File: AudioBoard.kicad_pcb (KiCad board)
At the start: 2 copper layers, 100 x 100 mm, 77 parts, among them IC1 AMS1117-5.0, IC2 PCM5102APWR, IC3 PCM1803ADBR, J1 I2S2_OPT, J10 POT, J11 POT, J12 Raspberry_Pi_2_3, J13 57PC5F, J14 57PC5F, J15 RCA_2x2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

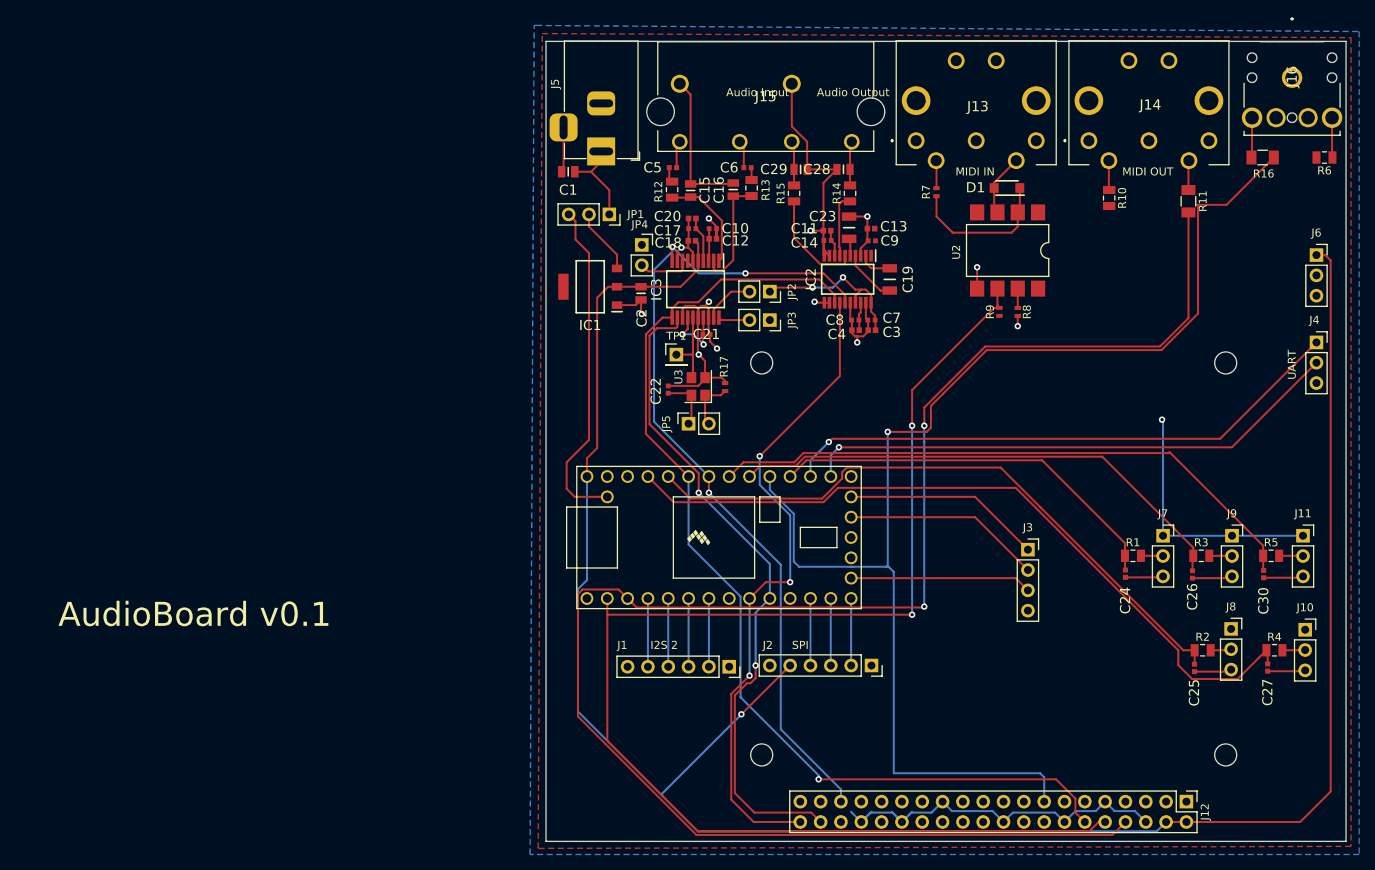
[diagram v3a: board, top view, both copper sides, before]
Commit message: Added mounting holes and wrapped up PCB design.
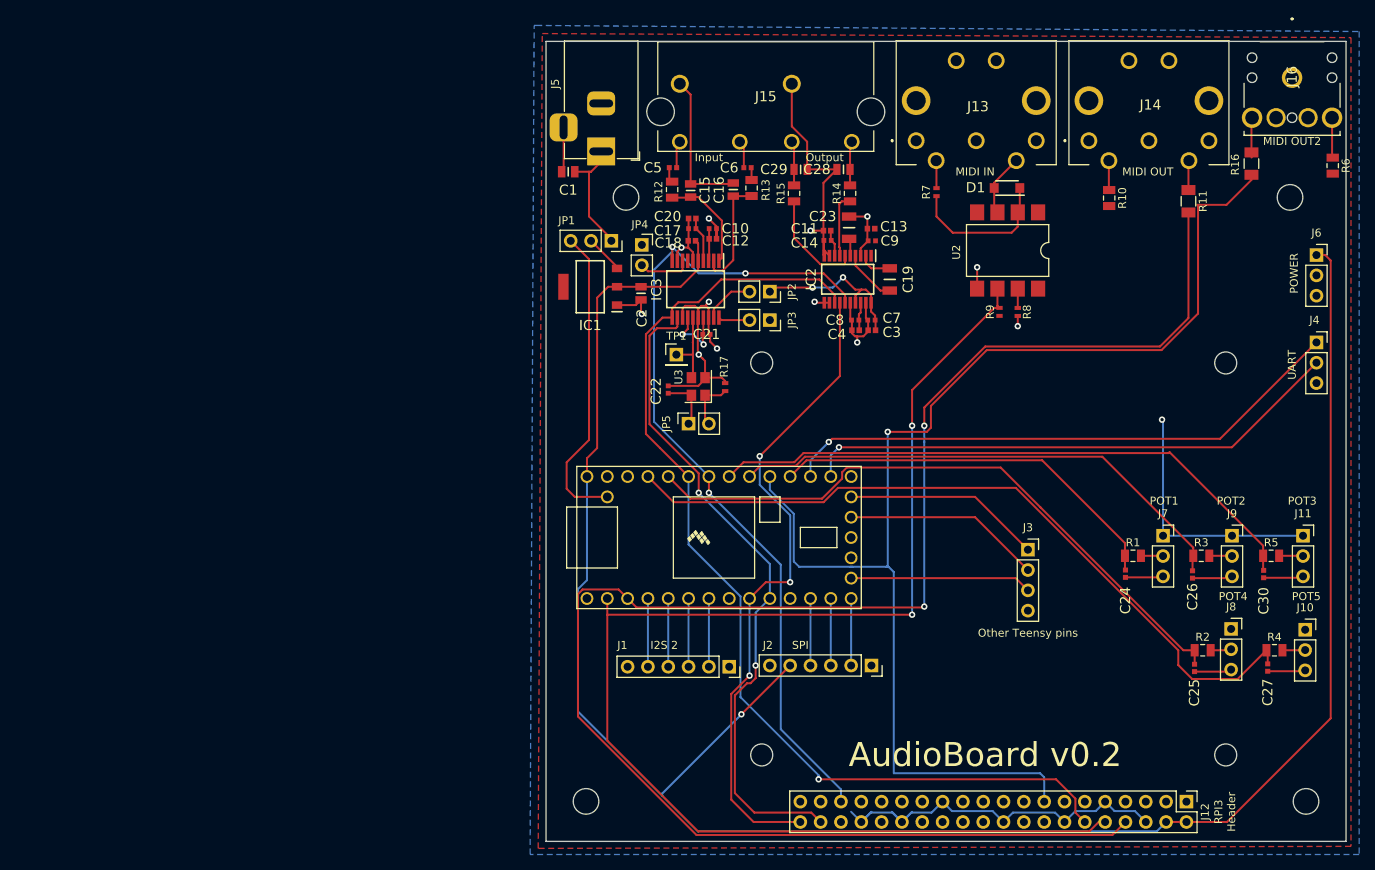
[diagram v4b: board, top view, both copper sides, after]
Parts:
- added REF**: MountingHole_3.2mm_M3, MountingHole:MountingHole_3.2mm_M3, F.Cu at (143.0, 69.5)
- added REF**: MountingHole_3.2mm_M3, MountingHole:MountingHole_3.2mm_M3, F.Cu at (60.0, 69.5)
- added REF**: MountingHole_3.2mm_M3, MountingHole:MountingHole_3.2mm_M3, F.Cu at (145.0, 145.0)
- added REF**: MountingHole_3.2mm_M3, MountingHole:MountingHole_3.2mm_M3, F.Cu at (55.0, 145.0)
- moved JP1 3.31 mm to (58.2, 74.9)
- moved R16 1.59 mm to (138.2, 65.3), turned to 270 degrees
- moved R6 1.45 mm to (148.3, 65.5), turned to 270 degrees
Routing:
- net +5V: track 264.2 -> 258.8 mm
- net /DC_IN: track 11.4 -> 14.9 mm
- net Net-(IC1-Pad3): track 8.20 -> 4.80 mm
- net /V_USB: track 42.0 -> 38.6 mm
- net /MIDI_OUT2: track 161.5 -> 158.2 mm
- net Net-(J16-Pad2): track 5.01 -> 4.49 mm
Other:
- board text added: "AudioBoard v0.2"
- board text added: "Input"
- board text added: "MIDI OUT2"
- board text added: "Other Teensy pins"
- board text added: "Output"
- board text added: "POT1"
- board text added: "POT2"
- board text added: "POT3"
- board text added: "POT4"
- board text added: "POT5"
- board text added: "POWER"
- board text added: "RPI3 Header"
- board text removed: "Audio Input"
- board text removed: "Audio Output"
- board text removed: "AudioBoard v0.1"

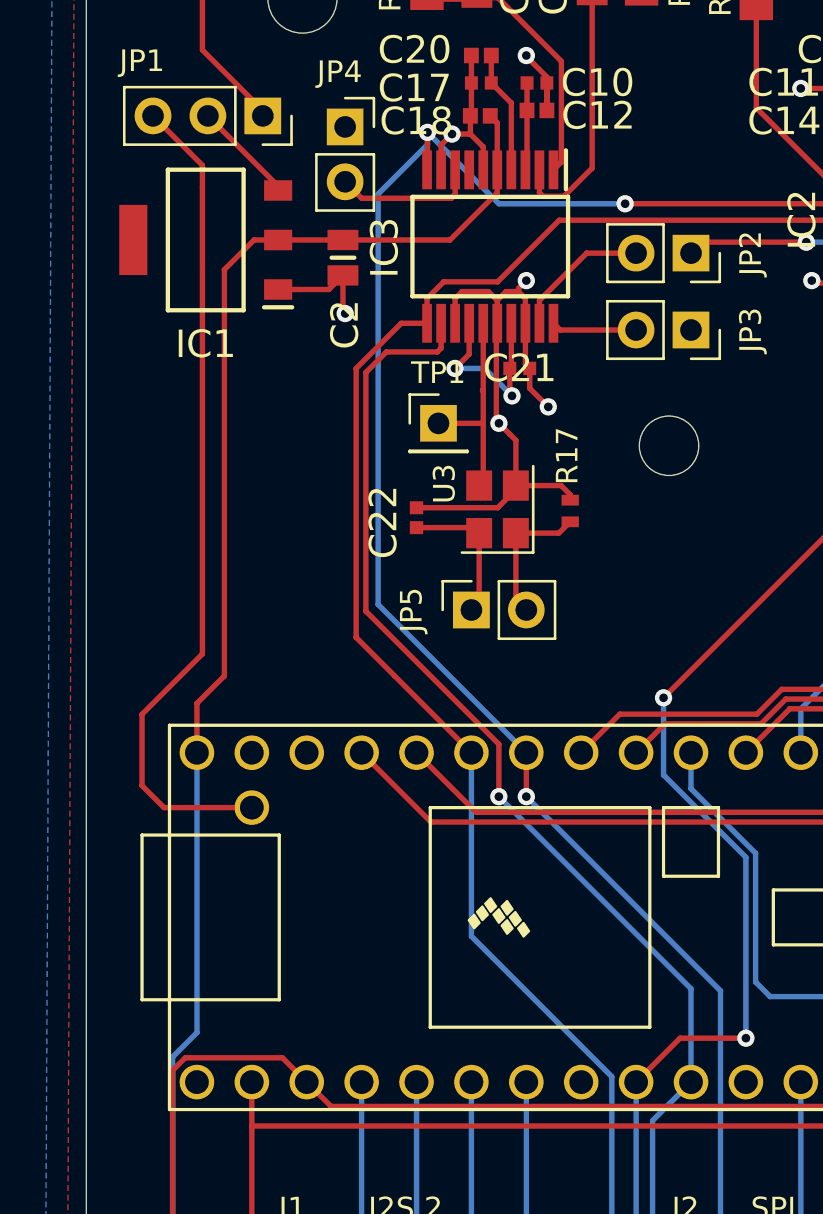
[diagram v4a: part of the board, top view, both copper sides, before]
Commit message: Added pin header for I2S input, to connect an external ADC (the PCM1803ADBR was unavailable at the time of ordering).
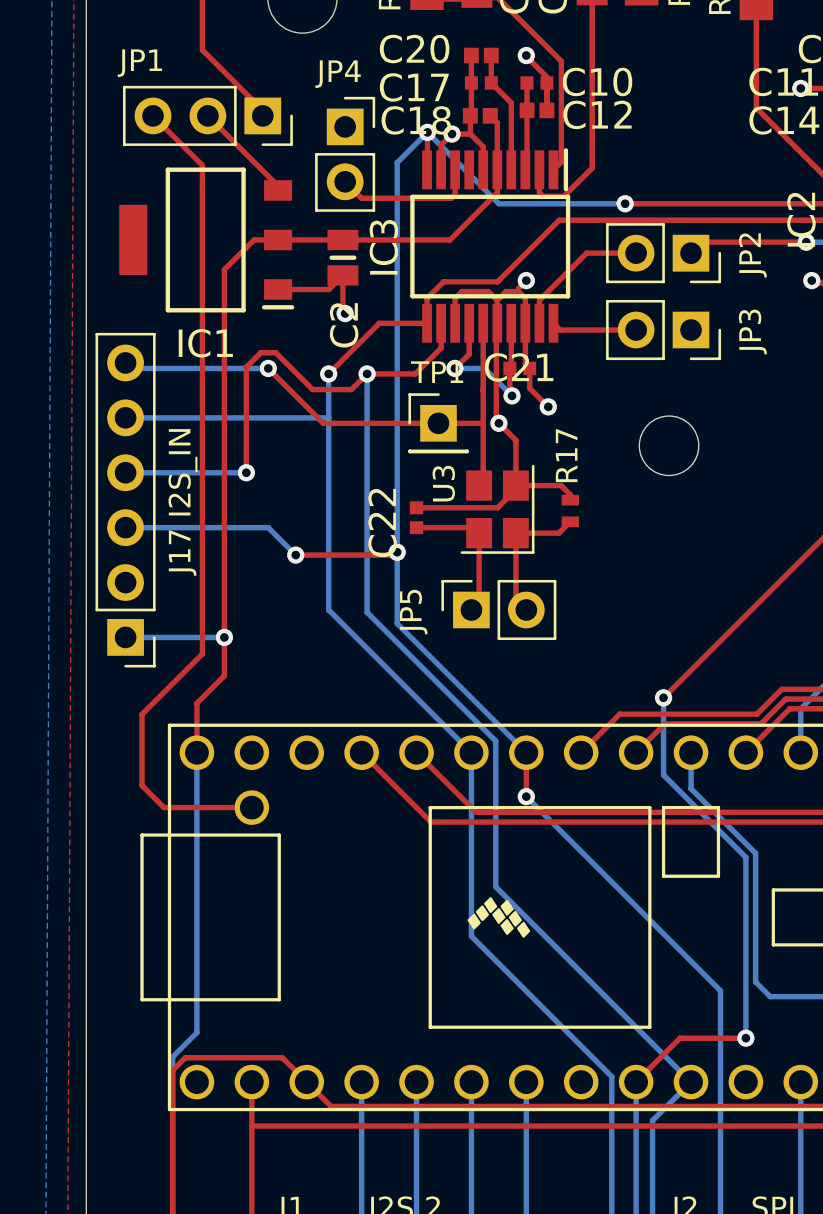
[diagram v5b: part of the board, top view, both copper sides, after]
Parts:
- added J17 I2S_IN: Conn_01x06, Connector_PinHeader_2.54mm:PinHeader_1x06_P2.54mm_Vertical, F.Cu at (51.8, 99.1)
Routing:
- net /I2S_DIN: track 82.8 -> 100.0 mm, vias 2 -> 3
- net /Audio IO (I2S)/SCK: track 9.73 -> 25.4 mm, vias 0 -> 1
- net /I2S_LRCK: track 106.8 -> 119.2 mm, vias 3 -> 5
- net /I2S_BCK: track 130.0 -> 141.0 mm, vias 1 -> 2
- net +5V: track 258.8 -> 263.4 mm, vias 1 -> 2
